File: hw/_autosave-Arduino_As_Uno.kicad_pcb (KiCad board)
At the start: 2 copper layers, 68.6 x 53.3 mm, 170 parts, among them CON1 BARREL_JACK, P1 USB_OTG, P10 CONN_01X06, P11 CONN_01X08, P13 CONN_02X03, P14 CONN_02X03_ICSP, P15 CONN_01X08, P2 CONN_02X03_ICSP, P22 CONN_02X03_ICSP, P3 CONN_02X03, P4 CONN_02X03_ICSP, P5 CONN_01X08, P6 CONN_02X03, P7 CONN_02X03_ICSP, P8 CONN_02X03_ICSP, P9 CONN_01X10, Q1 FDN340P, SW1 SW_PUSH, U1 LM2940LD-5.0, U10 TS3A44159, U11 FDG6331L, U2 MIC5205, U3 ATMEGA16U2, U4 23K256, U5 ATTINY85-SUR, U6 TS3A44159, U7 ATMEGA328PB-MU, U8 74LVCH1T45, U9 ATTINY85-SUR, X1 CRYSTAL, X2 RESONATOR

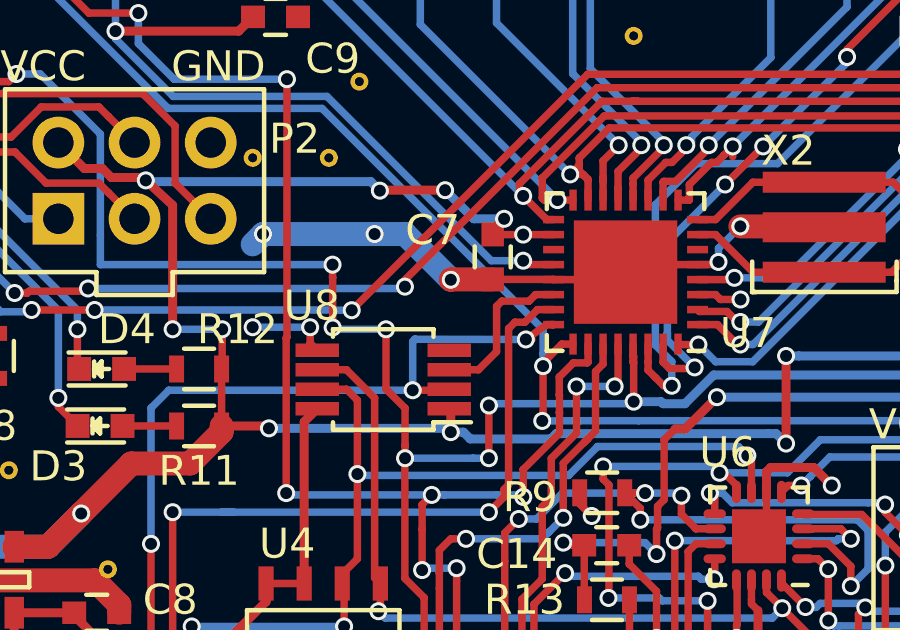
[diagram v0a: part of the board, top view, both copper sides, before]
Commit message: End of day commit. 12 Unconnected nets. Needs some silikscreen.
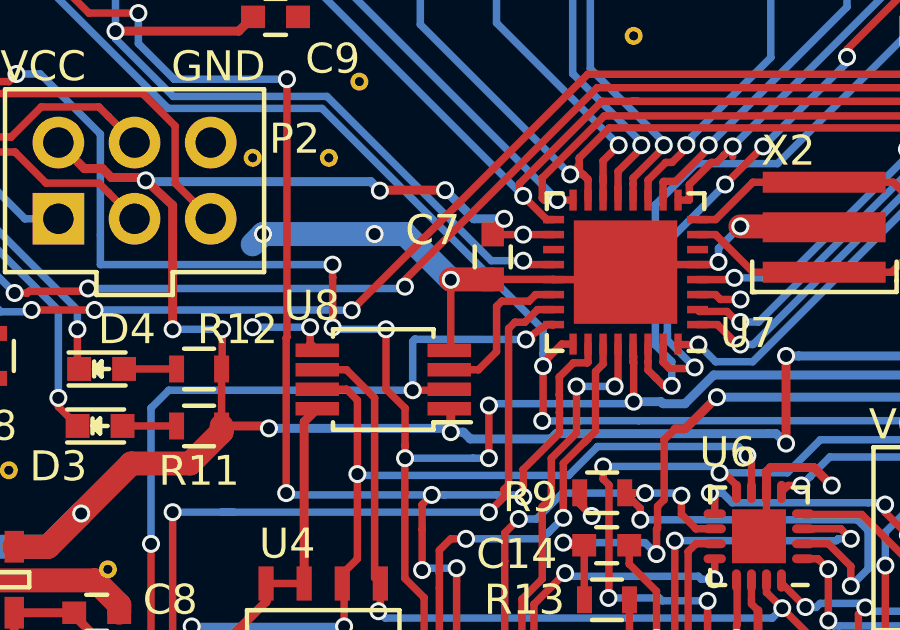
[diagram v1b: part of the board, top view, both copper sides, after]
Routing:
- net GND: track 74.4 -> 76.8 mm
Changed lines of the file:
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@@
 (kicad_pcb (version 4) (host pcbnew 4.0.2-stable)
   (general
-    (links 337)
-    (no_connects 8)
+    (links 338)
+    (no_connects 6)
     (area 110.922999 72.949999 179.653001 126.440001)
     (thickness 1.6)
     (drawings 22)
-    (tracks 1532)
+    (tracks 1534)
     (zones 0)
     (modules 170)
@@
   )
   (setup
-    (last_trace_width 0.25)
+    (last_trace_width 0.8)
     (user_trace_width 0.3)
     (user_trace_width 0.8)
@@
   (segment (start 114.99876 109.915) (end 117.298 109.915) (width 0.8) (layer F.Cu) (net 1))
   (segment (start 117.298 109.915) (end 118.998 111.615) (width 0.8) (layer F.Cu) (net 1))
+  (segment (start 146.05 88.265) (end 146.05 90.563) (width 0.25) (layer F.Cu) (net 2))
+  (segment (start 146.05 90.563) (end 145.998 90.615) (width 0.25) (layer F.Cu) (net 2))
   (segment (start 151.998 97.115) (end 151.998 97.74) (width 0.25) (layer F.Cu) (net 2))
   (via (at 152.908 100.203) (size 0.6) (drill 0.4) (layers F.Cu B.Cu) (net 2))
